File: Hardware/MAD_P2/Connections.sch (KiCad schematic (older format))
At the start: 44 parts, among them J10 Conn_02x05_Odd_Even, J11 Conn_02x05_Odd_Even, J13 Conn_02x05_Odd_Even, J14 Conn_02x05_Odd_Even, J15 Conn_ADC1, J16 Conn_DAC, J18 P3, J19 P4, J20 P2, J21 Conn_02x05_Odd_Even, J22 Conn_02x05_Odd_Even, J23 Conn_02x03_Odd_Even, J24 P5, J25 P6, J26 P7, J6 Edge_Conn, J7 Conn_02x05_Odd_Even, J8 USB_C_Receptacle_USB2.0, J9 Conn_02x05_Odd_Even, Q1 MMBT3904, U27 FT232RL

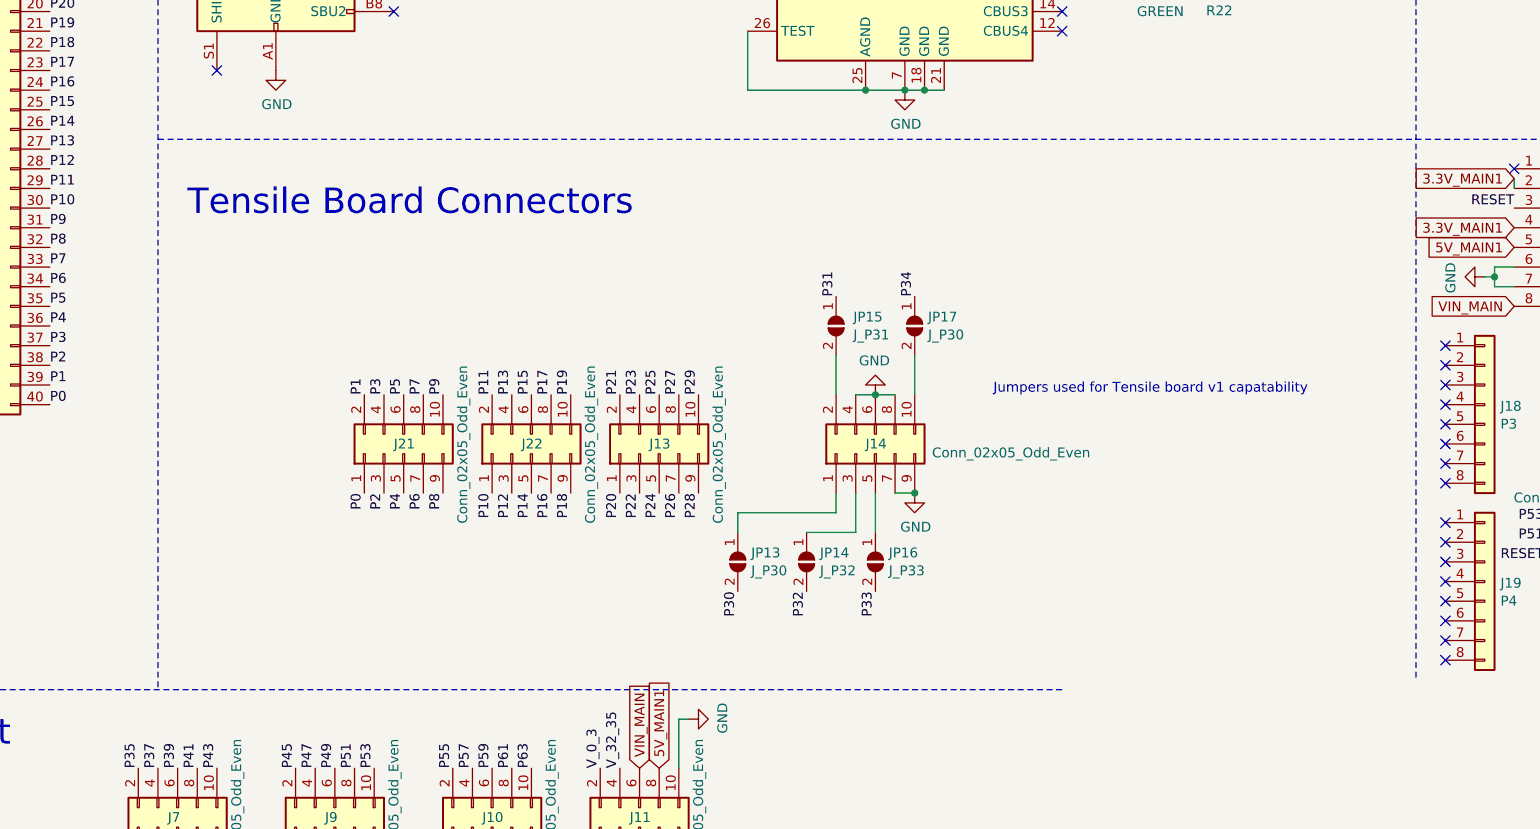
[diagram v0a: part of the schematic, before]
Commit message: added optional sd card socket for data
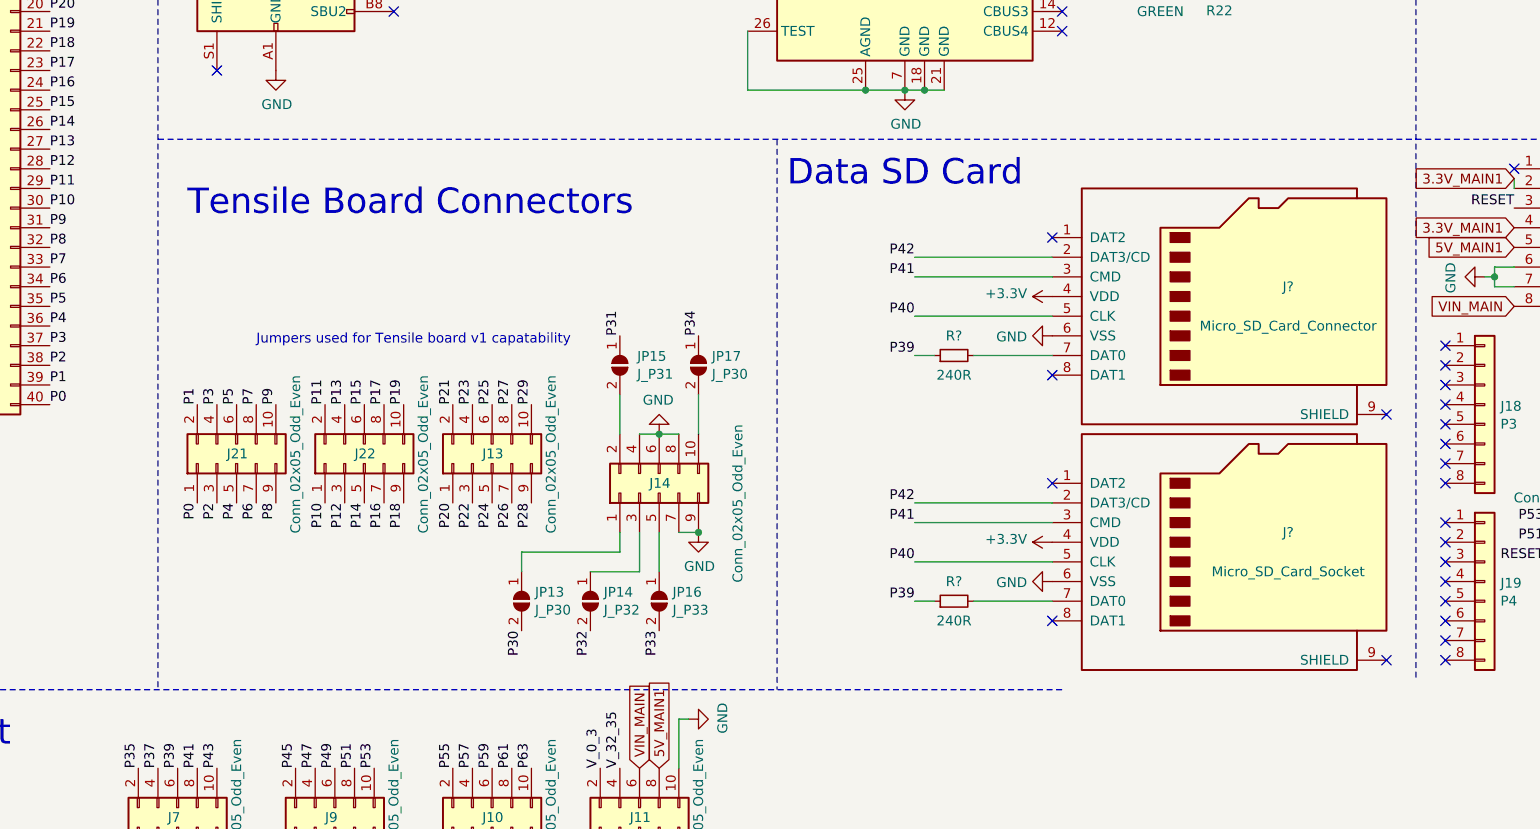
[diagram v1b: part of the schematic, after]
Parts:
- added J?: Micro_SD_Card_Connector, Tensile_Board:WM26501, symbol Connector:Micro_SD_Card
- added J?: Micro_SD_Card_Socket, Tensile_Board:WM26501, symbol Connector:Micro_SD_Card
- added R? (x2): 240R, Resistor_SMD:R_0603_1608Metric, symbol Device:R_Small
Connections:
- net GND: now also J?.6 (VSS), J?.6 (VSS)
- net P39: now also R?.1, R?.1
- net P40: now also J?.5 (CLK), J?.5 (CLK)
- net P41: now also J?.3 (CMD), J?.3 (CMD)
- net P42: now also J?.2 (DAT3/CD), J?.2 (DAT3/CD)
- new net: J?.7 (DAT0), R?.2 (x2)
- new net +3V3: J?.4 (VDD), J?.4 (VDD)
- no-connect marks 53 -> 59
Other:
- note added: "Data SD Card"
- moved on the sheet: J13, J14, J21, J22, JP13, JP14, JP15, JP16, JP17

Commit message: revising pcb layout
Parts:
- J32: renamed from J?; footprint Tensile_Board:WM26501 -> Connector_Card:microSD_HC_Hirose_DM3D-SF
- gave numbers to parts that had none: 3
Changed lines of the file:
@@
 P 7800 4550
 AR Path="/609BFBB9/612055B5" Ref="J?"  Part="1"
-AR Path="/60BD9EA1/612055B5" Ref="J?"  Part="1"
-F 0 "J?" H 8100 4600 50  0000 C CNN
+AR Path="/60BD9EA1/612055B5" Ref="J31"  Part="1"
+F 0 "J31" H 8100 4600 50  0000 C CNN
 F 1 "Micro_SD_Card_Connector" H 8100 4400 50  0000 C CNN
 F 2 "Tensile_Board:WM26501" H 8950 4850 50  0001 C CNN
@@
 U 1 1 612055BB
 P 6900 4550
-F 0 "#PWR?" H 6900 4400 50  0001 C CNN
+AR Path="/609BFBB9/612055BB" Ref="#PWR?"  Part="1"
+AR Path="/60BD9EA1/612055BB" Ref="#PWR0194"  Part="1"
+F 0 "#PWR0194" H 6900 4400 50  0001 C CNN
 F 1 "+3.3V" V 6915 4678 50  0000 L CNN
 F 2 "" H 6900 4550 50  0001 C CNN
@@
 U 1 1 612055C1
 P 6900 4750
-F 0 "#PWR?" H 6900 4500 50  0001 C CNN
+AR Path="/609BFBB9/612055C1" Ref="#PWR?"  Part="1"
+AR Path="/60BD9EA1/612055C1" Ref="#PWR0195"  Part="1"
+F 0 "#PWR0195" H 6900 4500 50  0001 C CNN
 F 1 "GND" V 6905 4622 50  0000 R CNN
 F 2 "" H 6900 4750 50  0001 C CNN
@@
 U 1 1 612055CA
 P 6400 4850
-F 0 "R?" V 6500 4850 50  0000 C CNN
+AR Path="/609BFBB9/612055CA" Ref="R?"  Part="1"
+AR Path="/60BD9EA1/612055CA" Ref="R35"  Part="1"
+F 0 "R35" V 6500 4850 50  0000 C CNN
 F 1 "240R" V 6300 4850 50  0000 C CNN
 F 2 "Resistor_SMD:R_0603_1608Metric" H 6400 4850 50  0001 C CNN
@@
 P 7800 5800
 AR Path="/609BFBB9/6120B790" Ref="J?"  Part="1"
-AR Path="/60BD9EA1/6120B790" Ref="J?"  Part="1"
-F 0 "J?" H 8100 5850 50  0000 C CNN
+AR Path="/60BD9EA1/6120B790" Ref="J32"  Part="1"
+F 0 "J32" H 8100 5850 50  0000 C CNN
 F 1 "Micro_SD_Card_Socket" H 8100 5650 50  0000 C CNN
-F 2 "Tensile_Board:WM26501" H 8950 6100 50  0001 C CNN
+F 2 "Connector_Card:microSD_HC_Hirose_DM3D-SF" H 8950 6100 50  0001 C CNN
 F 3 "http://katalog.we-online.de/em/datasheet/693072010801.pdf" H 7800 5800 50  0001 C CNN
 	1    7800 5800
@@
 U 1 1 6120B796
 P 6900 5800
-F 0 "#PWR?" H 6900 5650 50  0001 C CNN
+AR Path="/609BFBB9/6120B796" Ref="#PWR?"  Part="1"
+AR Path="/60BD9EA1/6120B796" Ref="#PWR0196"  Part="1"
+F 0 "#PWR0196" H 6900 5650 50  0001 C CNN
 F 1 "+3.3V" V 6915 5928 50  0000 L CNN
 F 2 "" H 6900 5800 50  0001 C CNN
@@
 U 1 1 6120B79C
 P 6900 6000
-F 0 "#PWR?" H 6900 5750 50  0001 C CNN
+AR Path="/609BFBB9/6120B79C" Ref="#PWR?"  Part="1"
+AR Path="/60BD9EA1/6120B79C" Ref="#PWR0197"  Part="1"
+F 0 "#PWR0197" H 6900 5750 50  0001 C CNN
 F 1 "GND" V 6905 5872 50  0000 R CNN
 F 2 "" H 6900 6000 50  0001 C CNN
@@
 U 1 1 6120B7A5
 P 6400 6100
-F 0 "R?" V 6500 6100 50  0000 C CNN
+AR Path="/609BFBB9/6120B7A5" Ref="R?"  Part="1"
+AR Path="/60BD9EA1/6120B7A5" Ref="R36"  Part="1"
+F 0 "R36" V 6500 6100 50  0000 C CNN
 F 1 "240R" V 6300 6100 50  0000 C CNN
 F 2 "Resistor_SMD:R_0603_1608Metric" H 6400 6100 50  0001 C CNN

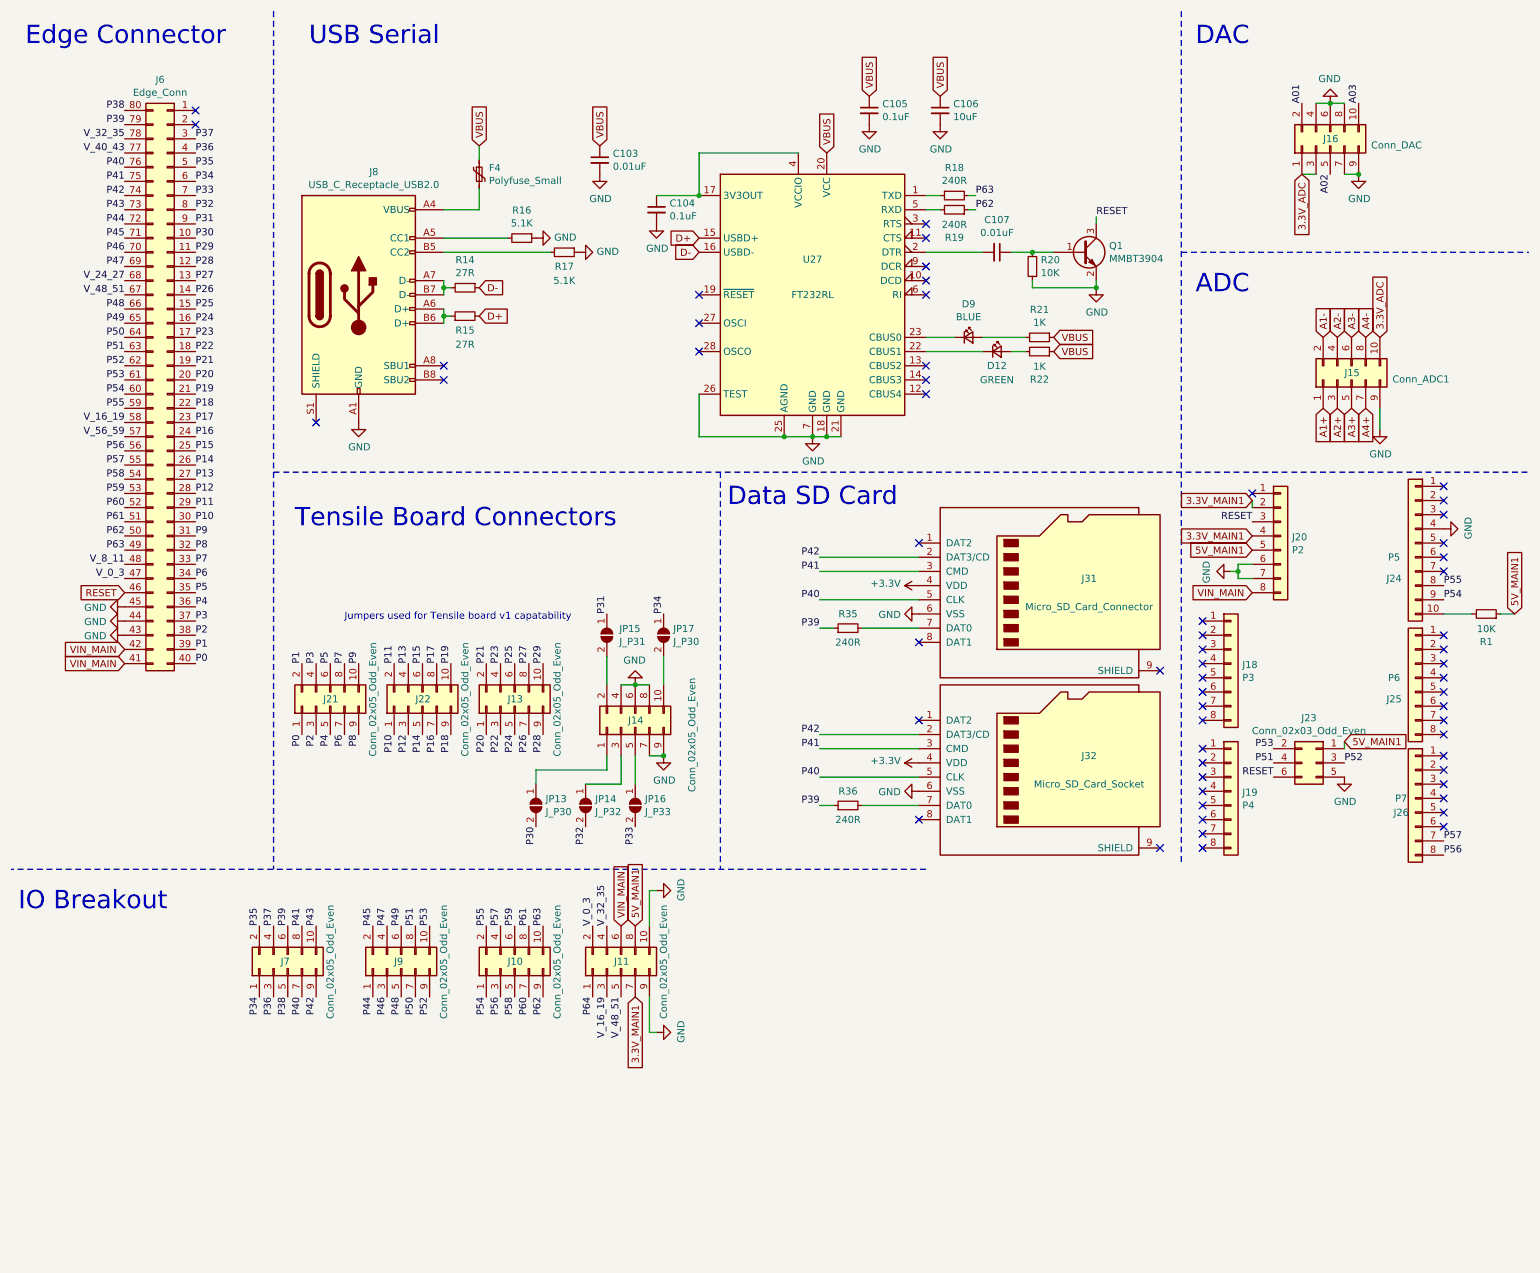
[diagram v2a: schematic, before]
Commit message: routed adc
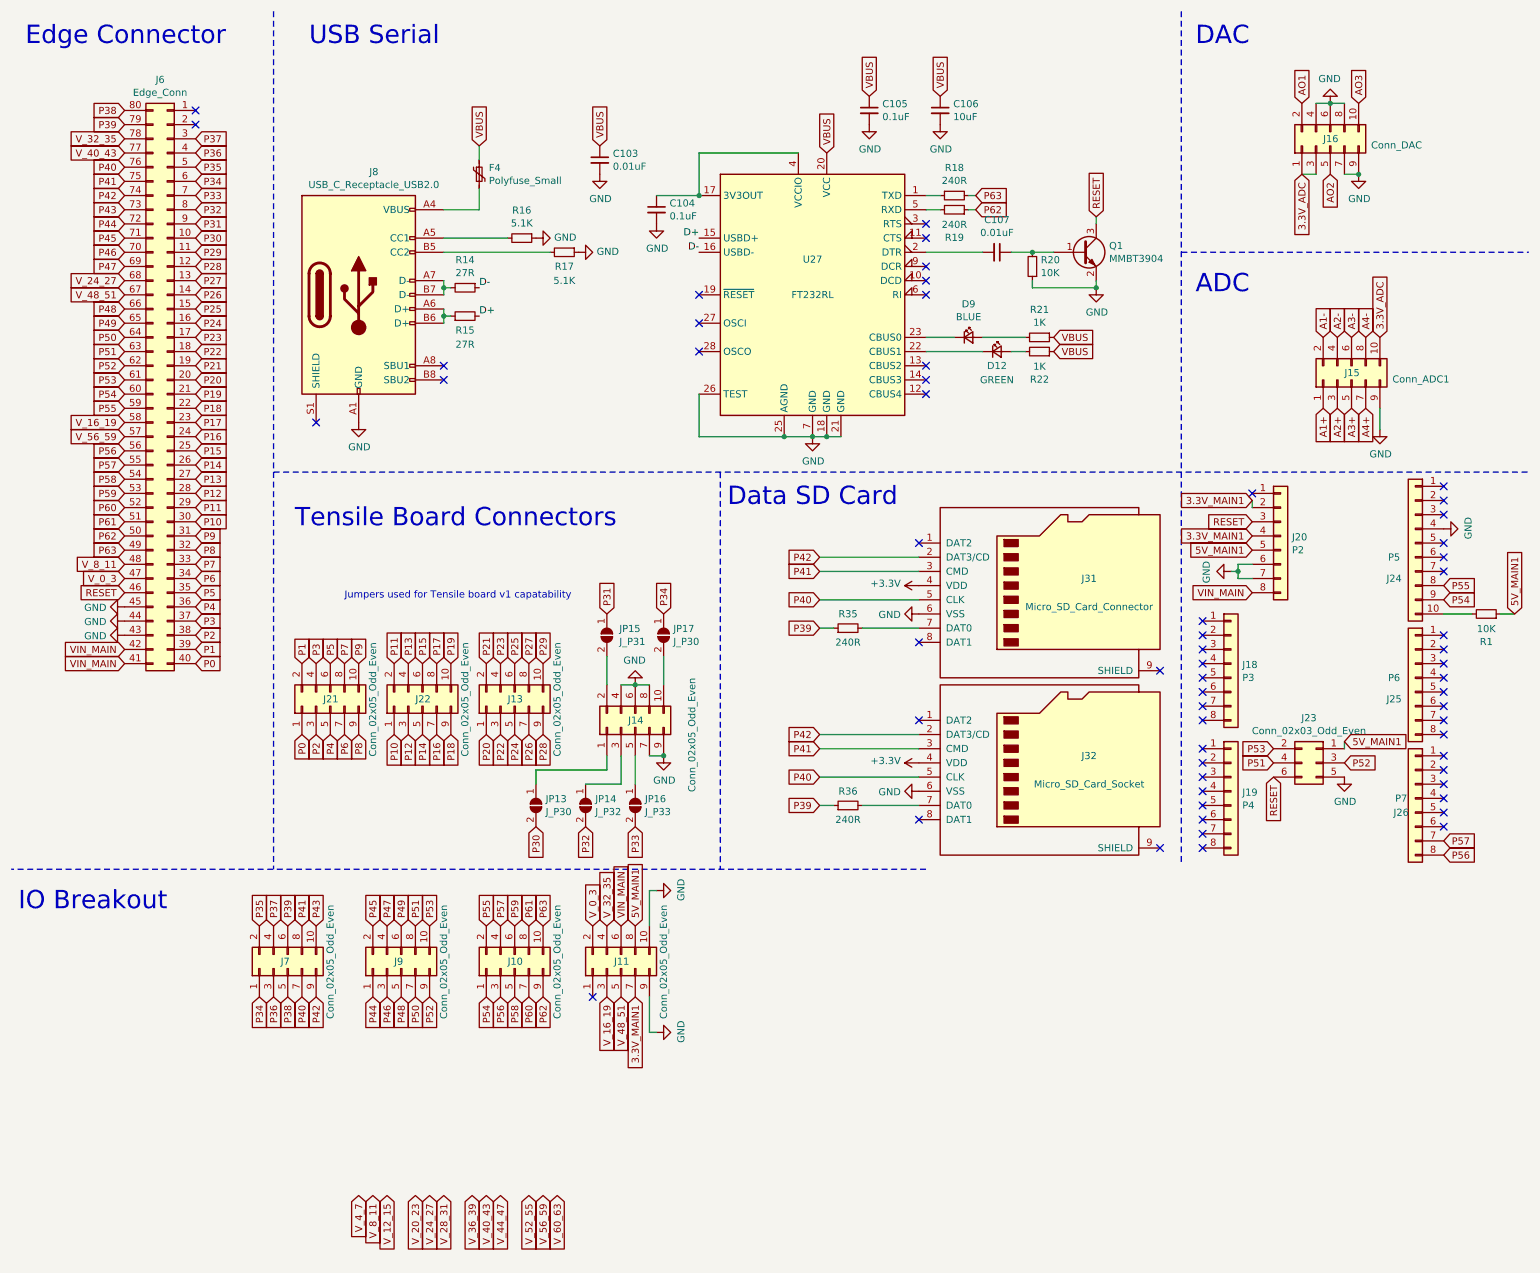
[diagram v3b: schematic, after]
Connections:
- net A01 renamed AO1
- net A02 renamed AO2
- net A03 renamed AO3
- net P64: no longer names the net of J11.1 (Pin_1)
- no-connect marks 59 -> 60

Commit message: test
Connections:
- net 3.3V_ADC: no longer J16.3 (Pin_3)
- new net 5V_ADC: J16.3 (Pin_3)
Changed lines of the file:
@@
 $EndComp
-Wire Wire Line
-	9600 1650 9700 1650
 Wire Wire Line
 	9900 1650 10000 1650
@@
 Text GLabel 6200 6100 0    50   Input ~ 0
 P39
+Text GLabel 9700 1650 3    50   Input ~ 0
+5V_ADC
 $EndSCHEMATC

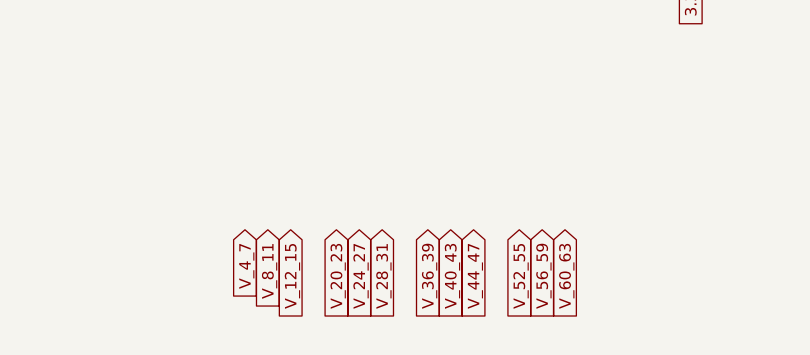
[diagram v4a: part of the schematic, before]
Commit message: changed to 4 layer board due to number of wires to route. Routed ground and power nets
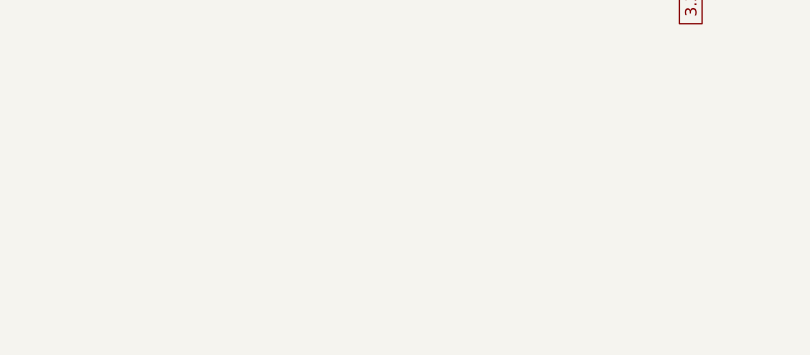
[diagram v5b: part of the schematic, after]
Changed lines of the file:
@@
 Text GLabel 4600 6950 1    50   Input ~ 0
 V_0_3
-Text GLabel 2950 8850 3    50   Input ~ 0
-V_4_7
-Text GLabel 3050 8850 3    50   Input ~ 0
-V_8_11
-Text GLabel 3150 8850 3    50   Input ~ 0
-V_12_15
-Text GLabel 3350 8850 3    50   Input ~ 0
-V_20_23
 Text GLabel 4700 7450 3    50   Input ~ 0
 V_16_19
-Text GLabel 3450 8850 3    50   Input ~ 0
-V_24_27
-Text GLabel 3550 8850 3    50   Input ~ 0
-V_28_31
 Text GLabel 4700 6950 1    50   Input ~ 0
 V_32_35
-Text GLabel 3750 8850 3    50   Input ~ 0
-V_36_39
-Text GLabel 3850 8850 3    50   Input ~ 0
-V_40_43
-Text GLabel 3950 8850 3    50   Input ~ 0
-V_44_47
 Text GLabel 4800 7450 3    50   Input ~ 0
 V_48_51
-Text GLabel 4150 8850 3    50   Input ~ 0
-V_52_55
-Text GLabel 4250 8850 3    50   Input ~ 0
-V_56_59
-Text GLabel 4350 8850 3    50   Input ~ 0
-V_60_63
 NoConn ~ 4600 7450
 Text GLabel 5100 4750 1    50   Input ~ 0

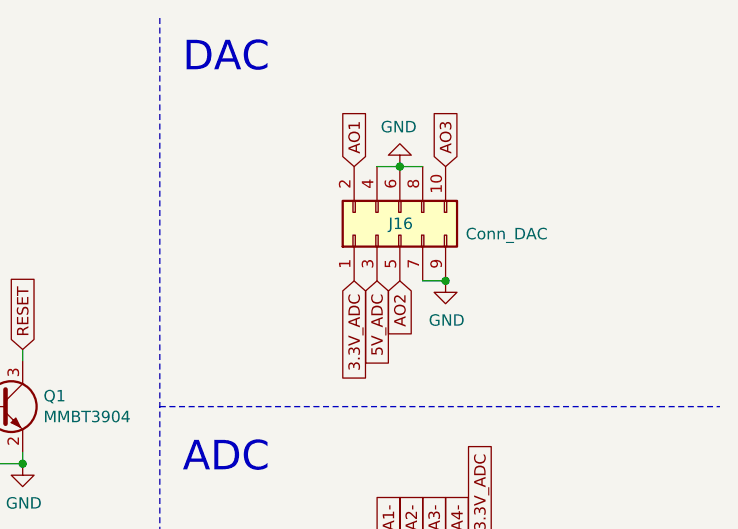
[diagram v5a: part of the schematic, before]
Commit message: fixed DAC issue and added silkscreen
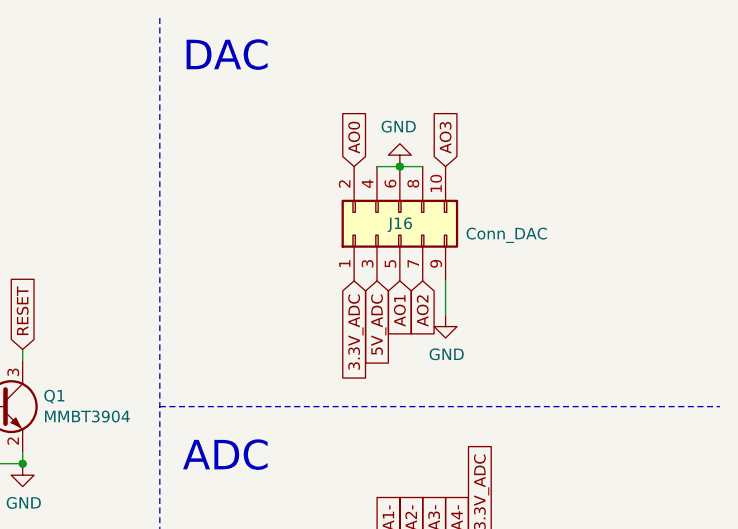
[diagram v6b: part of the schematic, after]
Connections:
- net AO1: now also J16.5 (Pin_5); no longer J16.2 (Pin_2)
- net AO2: now also J16.7 (Pin_7); no longer J16.5 (Pin_5)
- net GND: no longer J16.7 (Pin_7)
- new net AO0: J16.2 (Pin_2)
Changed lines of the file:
@@
 L power:GND #PWR?
 U 1 1 60DE4CD9
-P 10000 1650
+P 10000 1800
 AR Path="/609BFBB9/60DE4CD9" Ref="#PWR?"  Part="1"
 AR Path="/60C11A52/60DE4CD9" Ref="#PWR?"  Part="1"
 AR Path="/60BD9EA1/60DE4CD9" Ref="#PWR0219"  Part="1"
-F 0 "#PWR0219" H 10000 1400 50  0001 C CNN
-F 1 "GND" H 10005 1477 50  0000 C CNN
-F 2 "" H 10000 1650 50  0001 C CNN
-F 3 "" H 10000 1650 50  0001 C CNN
-	1    10000 1650
+F 0 "#PWR0219" H 10000 1550 50  0001 C CNN
+F 1 "GND" H 10005 1627 50  0000 C CNN
+F 2 "" H 10000 1800 50  0001 C CNN
+F 3 "" H 10000 1800 50  0001 C CNN
+	1    10000 1800
 	1    0    0    -1
 $EndComp
-Wire Wire Line
-	9900 1650 10000 1650
-Connection ~ 10000 1650
 $Comp
 L power:GND #PWR?
@@
 Text GLabel 8150 1950 1    50   Input ~ 0
 RESET
-Text GLabel 9600 1150 1    50   Input ~ 0
+Text GLabel 9800 1650 3    50   Input ~ 0
 AO1
 Text GLabel 10000 1150 1    50   Input ~ 0
 AO3
-Text GLabel 9800 1650 3    50   Input ~ 0
+Text GLabel 9900 1650 3    50   Input ~ 0
 AO2
 Text GLabel 9250 4100 0    50   Input ~ 0
@@
 Text GLabel 9700 1650 3    50   Input ~ 0
 5V_ADC
+Text GLabel 9600 1150 1    50   Input ~ 0
+AO0
+Wire Wire Line
+	10000 1650 10000 1800
 $EndSCHEMATC
